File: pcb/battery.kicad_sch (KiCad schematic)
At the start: 27 parts, among them Q2 AO3401A, Q3 AO3401A, Q4 AO3401A, Q5 AO3400A, Q6 AO3400A, Q7 AO3401A, Q8 AO3400A, SW1 Power, U3 TP4056

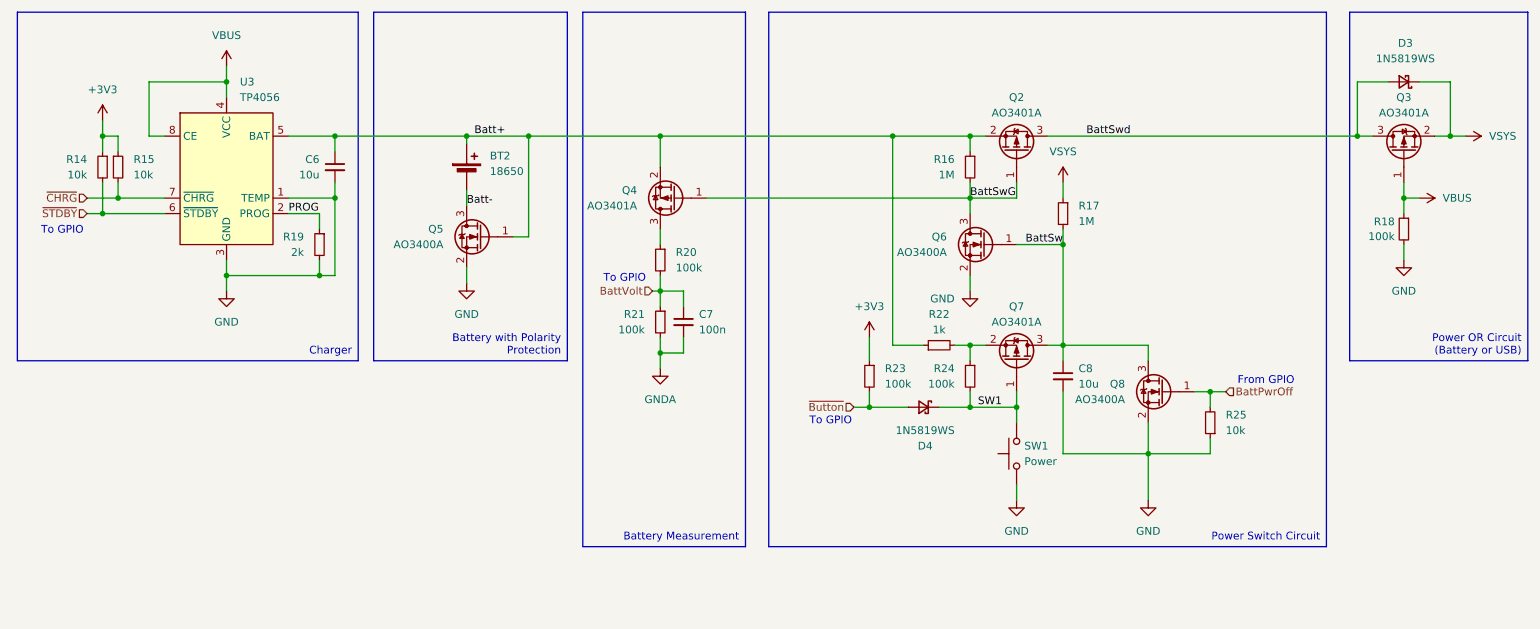
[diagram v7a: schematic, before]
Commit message: fix: move measurement to BattSwd
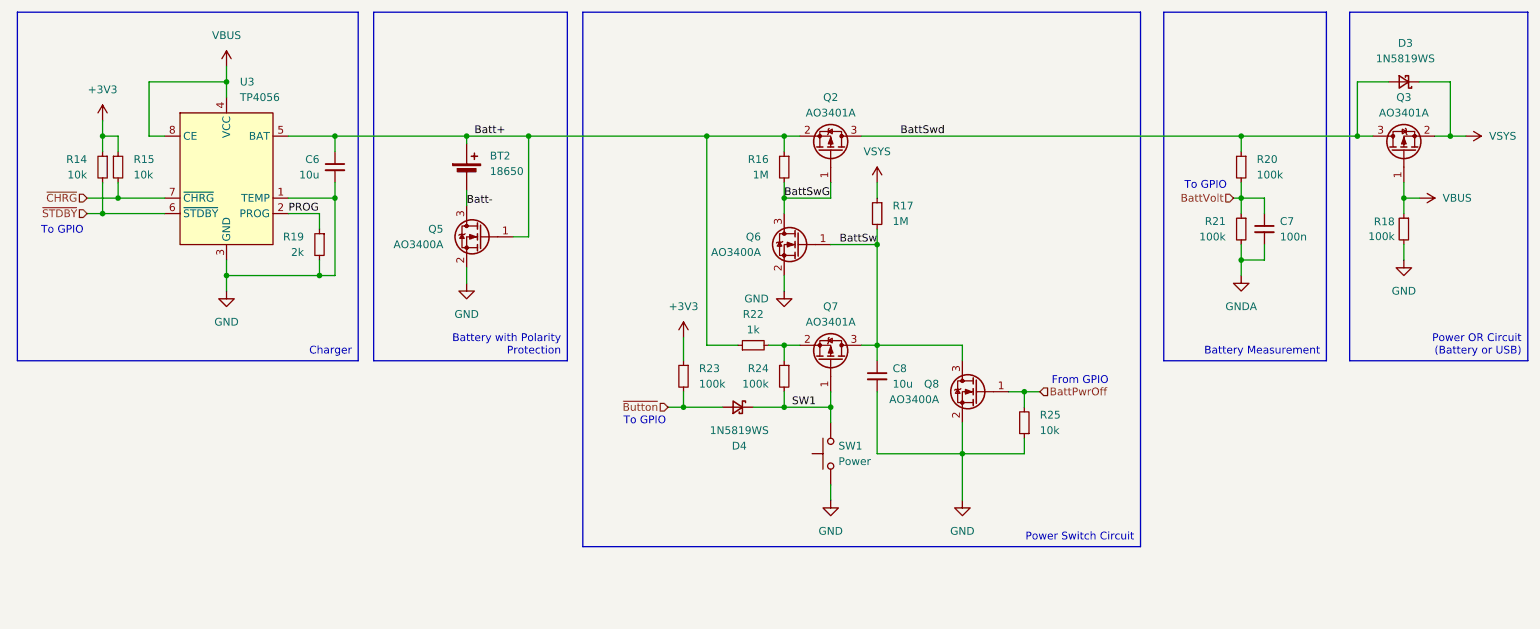
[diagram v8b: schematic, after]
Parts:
- removed Q4: AO3401A, Package_TO_SOT_SMD:SOT-23, symbol Transistor_FET:AO3401A
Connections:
- net BattSwd: now also R20.1
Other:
- moved on the sheet: C7, C8, D4, Q2, Q6, Q7, Q8, R16, R17, R20, R21, R22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
